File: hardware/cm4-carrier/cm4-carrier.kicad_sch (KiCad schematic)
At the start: 0 parts

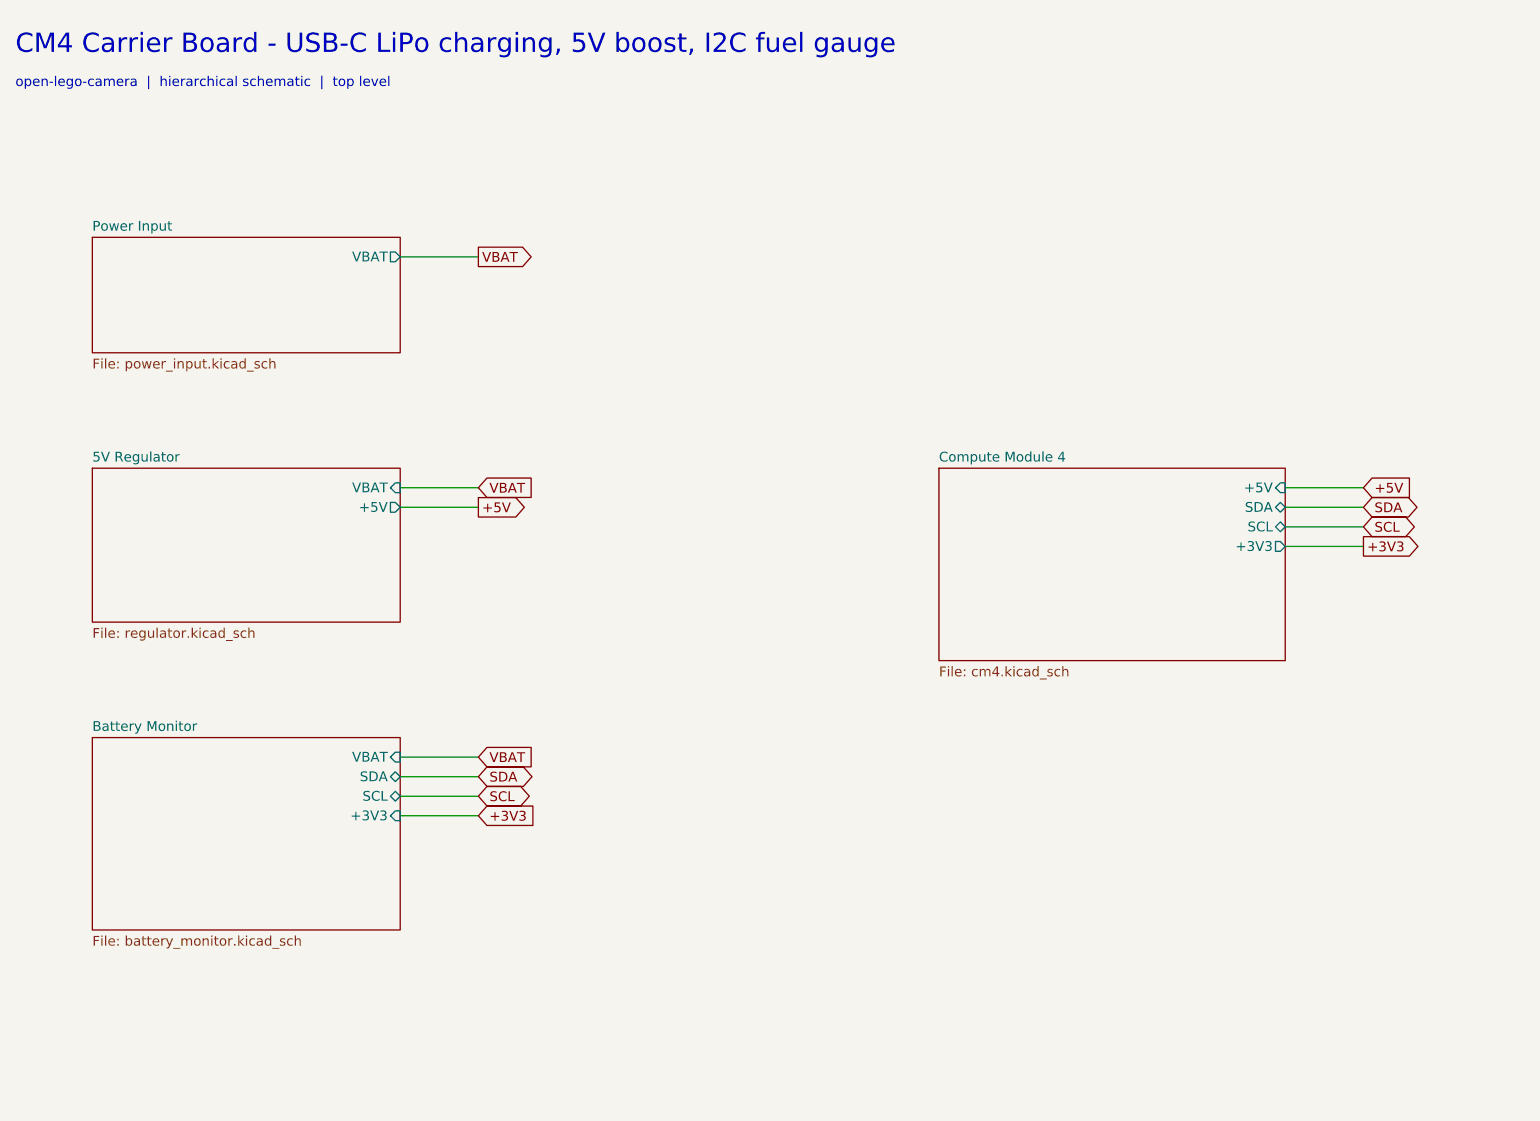
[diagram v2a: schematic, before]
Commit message: Add Dynamic Power Path Management and battery protection
Rework the power architecture to add DPPM and dedicated cell protection.

Power path (DPPM): replace the MCP73831 with a TI BQ24075 USB-friendly
charger whose OUT pin is a separate system rail (SYS). The load now runs
directly from USB when present (system works with a dead/absent battery and
the cell is not needlessly cycled) and falls back to the battery when USB is
removed, while the cell charges from the remaining input budget. Adds ISET,
ILIM and TMR programming resistors, EN1/EN2/CE/SYSOFF strapping, a 10k NTC
on TS for battery-temperature protection, and CHG/PGOOD status LEDs. The
5 V boost regulator now draws from SYS instead of VBAT.

Battery protection: new battery_protection.kicad_sch sub-sheet with an
AP9101CK6 1-cell protection controller (DW01A-class) driving an FS8205A dual
N-MOSFET in the cell's negative line — over-charge, over-discharge,
over-current and short-circuit cutoff. The raw JST cell connector moves here;
its protected terminals feed VBAT/GND to the rest of the board.

Pinouts for BQ24075 and AP9101CK6 were taken from KiCad's Battery_Management
library. Root sheet gains the Battery Protection box and the SYS net; all
hierarchical labels match their sheet pins and reference designators are
globally unique. README/BOM updated. No format change (KiCad 10, 20260306).

Co-Authored-By: Claude Opus 4.8 <noreply@anthropic.com>
Claude-Session: https://claude.ai/code/session_015B7X7FE461jFSRaiTFdnFt
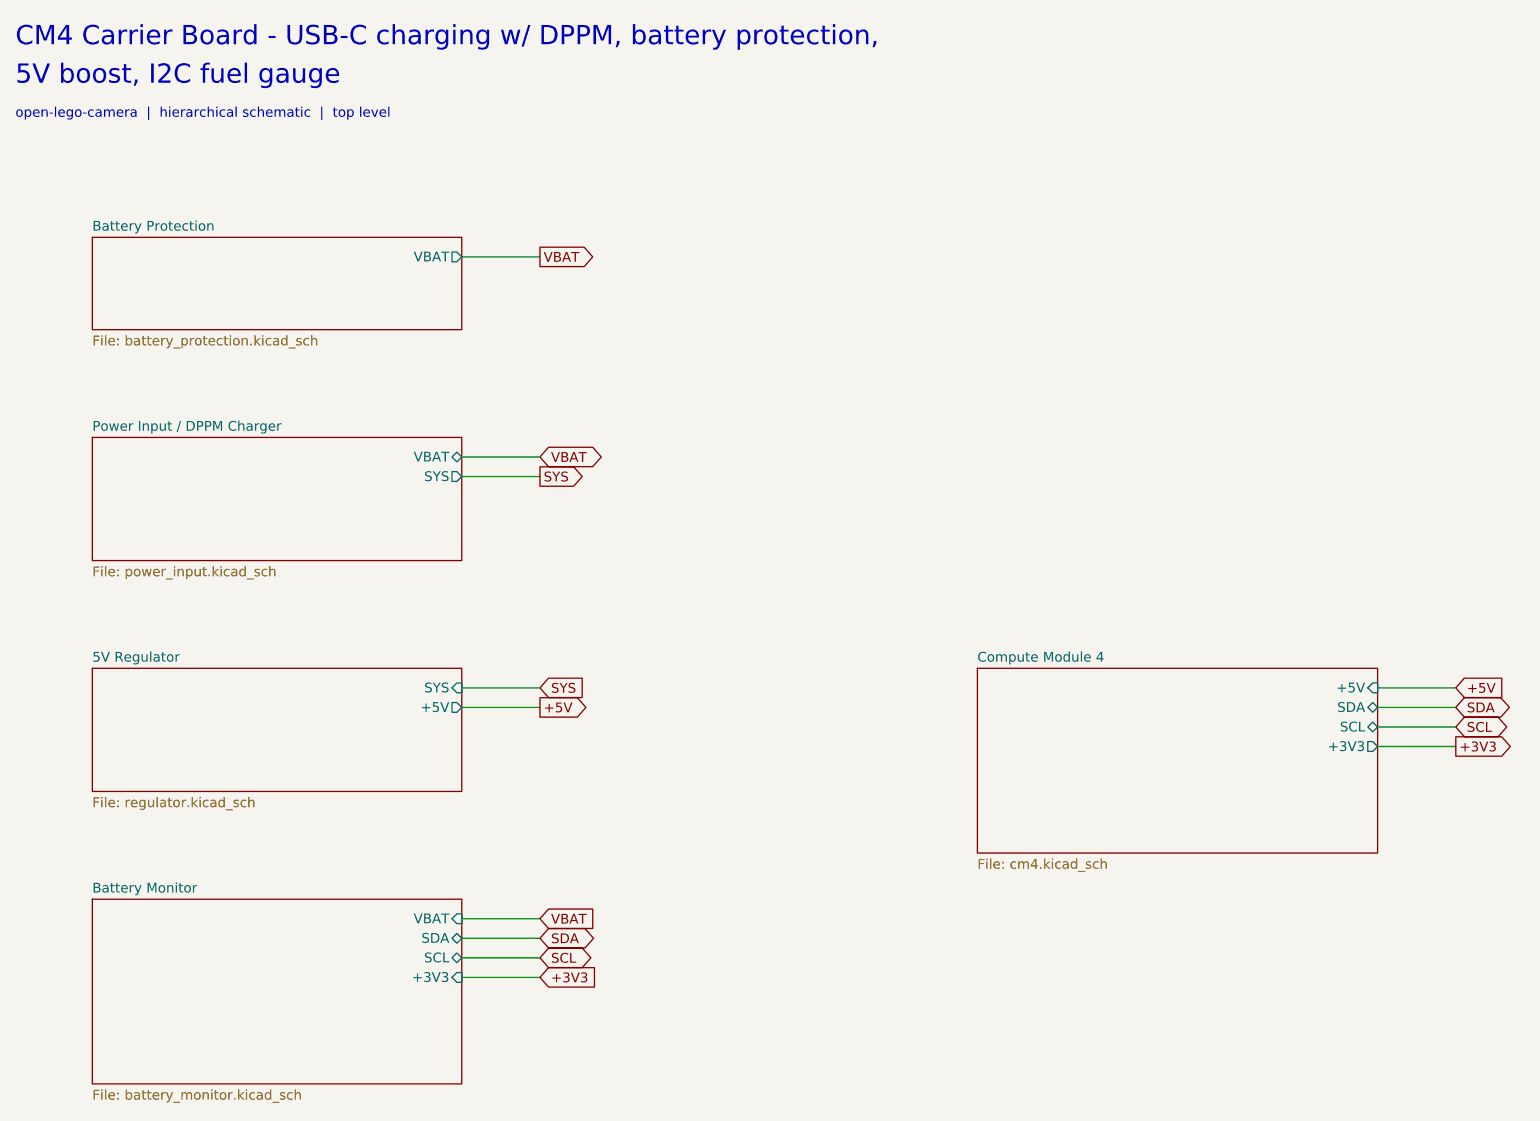
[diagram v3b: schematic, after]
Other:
- removed sheet Power Input
- added sheet Battery Protection (battery_protection.kicad_sch)
- added sheet Power Input / DPPM Charger (power_input.kicad_sch)
- sheet 5V Regulator ports: added SYS; removed VBAT
- note added: "5V boost, I2C fuel gauge"
- note added: "CM4 Carrier Board - USB-C charging w/ DPPM, battery protection,"
- note removed: "CM4 Carrier Board - USB-C LiPo charging, 5V boost, I2C fuel gauge"

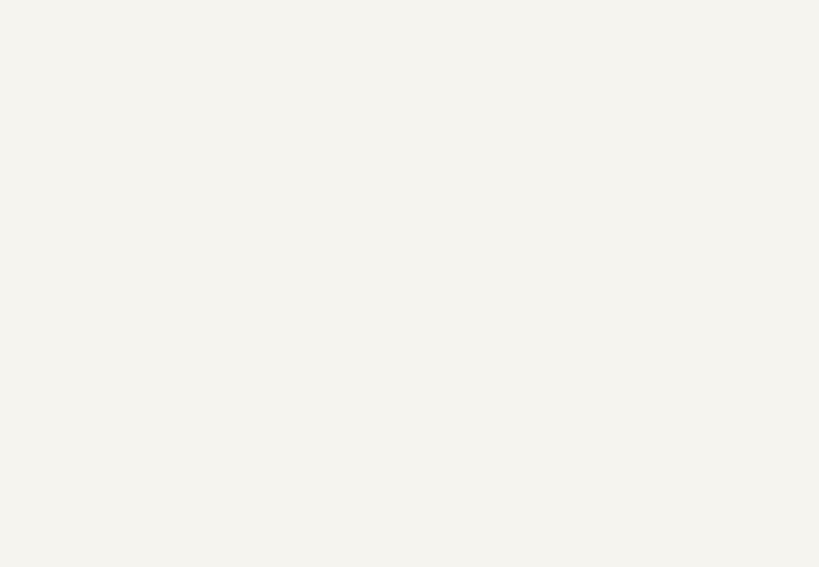
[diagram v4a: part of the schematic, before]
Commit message: Add two CSI-2 cameras with I2C mux and camera 3.3V rail
Add a new cameras.kicad_sch sub-sheet providing two Raspberry Pi CSI-2 camera
interfaces:

- J5 (CSI Camera 0) on the CM4's CAM0 (2-lane) interface; J6 (CSI Camera 1)
  on CAM1 (4-lane, two lanes wired) — standard 15-pin 1.0mm Pi camera FFC
  connectors (Connector_FFC-FPC:JUSHUO_AFA07-S15FCA-00...).
- PCA9544A I2C mux (U5) on the camera control bus I2C0 so the two identical-
  address sensors each sit on their own downstream channel (cam0 = ch0,
  cam1 = ch1, mux at 0x70).
- AP2112K-3.3 LDO (U7) generating a dedicated camera 3.3V rail from +5V, so
  two cameras don't overload the CM4's limited CM4_3.3V_Out. Adds per-channel
  and upstream I2C pull-ups and decoupling (R15-R20, C13-C15).

The CM4 sheet now exports the CAM0/CAM1 MIPI lanes (from J4), I2C0
(I2C_SCL0/SDA0) and four spare GPIOs (GPIO4-7, for the camera IO0/IO1
LED/enable lines) as global nets; the cameras sheet consumes them. Camera
FFC pinout and PCA9544A/DF40/FFC footprints were taken from KiCad's
libraries and the standard 15-pin CSI pinout.

Root gains a (pinless) Cameras sheet box. README/BOM updated. No
schematic-format change (KiCad 10, 20260306).

Co-Authored-By: Claude Opus 4.8 <noreply@anthropic.com>
Claude-Session: https://claude.ai/code/session_015B7X7FE461jFSRaiTFdnFt
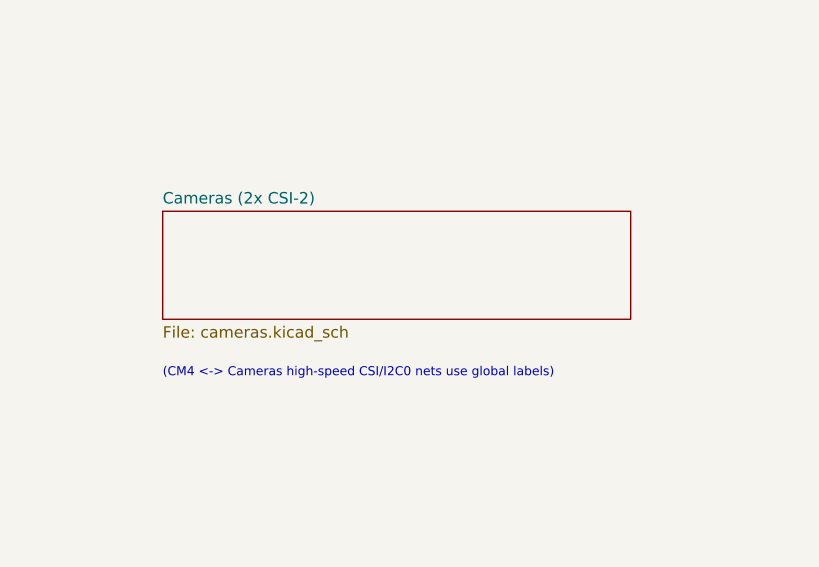
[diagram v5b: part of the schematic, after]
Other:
- added sheet Cameras (2x CSI-2) (cameras.kicad_sch)
- note added: "(CM4 <-> Cameras high-speed CSI/I2C0 nets use global labels)"
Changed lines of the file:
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@@
 		(instances
 			(project "cm4-carrier"
-				(path "/38639fc7-8081-4077-bac3-dd3ee57cf696"
+				(path "/5261f1c5-8601-4e00-981c-a52873d90ff9"
 					(page "6"))))
 	)
@@
 		(instances
 			(project "cm4-carrier"
-				(path "/38639fc7-8081-4077-bac3-dd3ee57cf696"
+				(path "/5261f1c5-8601-4e00-981c-a52873d90ff9"
 					(page "2"))))
 	)
@@
 		(instances
 			(project "cm4-carrier"
-				(path "/38639fc7-8081-4077-bac3-dd3ee57cf696"
+				(path "/5261f1c5-8601-4e00-981c-a52873d90ff9"
 					(page "3"))))
 	)
@@
 		(instances
 			(project "cm4-carrier"
-				(path "/38639fc7-8081-4077-bac3-dd3ee57cf696"
+				(path "/5261f1c5-8601-4e00-981c-a52873d90ff9"
 					(page "4"))))
 	)
@@
 		(instances
 			(project "cm4-carrier"
-				(path "/38639fc7-8081-4077-bac3-dd3ee57cf696"
+				(path "/5261f1c5-8601-4e00-981c-a52873d90ff9"
 					(page "5"))))
 	)
+	(sheet (at 155.00 40.00) (size 52.00 12.00)
+		(exclude_from_sim no) (in_bom yes) (on_board yes) (dnp no)
+		(fields_autoplaced yes)
+		(stroke (width 0.1524) (type solid))
+		(fill (color 0 0 0 0.0000))
+		(property "Sheetname" "Cameras (2x CSI-2)" (at 155.00 39.29 0)
+			(effects (font (size 1.27 1.27)) (justify left bottom)))
+		(property "Sheetfile" "cameras.kicad_sch" (at 155.00 52.71 0)
+			(effects (font (size 1.27 1.27)) (justify left top)))
+		(instances
+			(project "cm4-carrier"
+				(path "/5261f1c5-8601-4e00-981c-a52873d90ff9"
+					(page "7"))))
+	)
+	(text "(CM4 <-> Cameras high-speed CSI/I2C0 nets use global labels)" (at 155.00 58.00 0)
+		(effects (font (size 1.0 1.0)) (justify left))
+)
 	(wire (pts (xy 88.00 42.54) (xy 98.16 42.54))
 		(stroke (width 0) (type default))

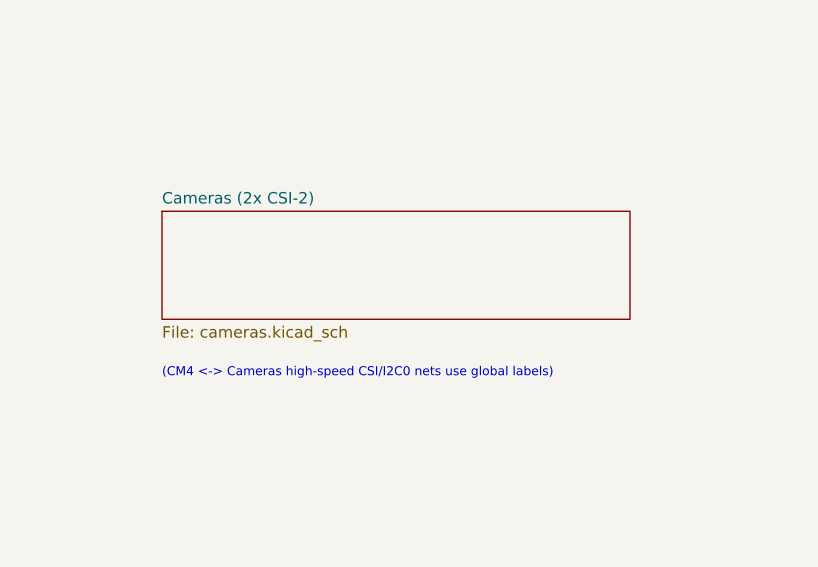
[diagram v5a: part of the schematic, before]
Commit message: Add a DSI display on the CM4's DSI0 interface
Add a Raspberry Pi DSI display connector (J7) to the peripherals sheet
(now "Cameras & Display"):

- J7 is a standard 15-pin 1.0mm RPi FFC driven by the CM4's DSI0 (2-lane)
  interface; the six DSI0 differential lanes are exported from the CM4 sheet
  (J4) as global nets alongside the camera lanes.
- The display's touch/controller I2C shares I2C0 on PCA9544A mux channel 2
  (SD2/SC2, previously unused), with its own pull-ups (R21/R22).
- IO0/IO1 (reset / backlight-enable) route to CM4 GPIO8/GPIO9; 3.3V logic
  comes from the existing camera LDO rail. The 5V panel/backlight power is
  supplied separately, as on the standard RPi 7-inch panel.

The mux is now 3 of 4 channels used (cam0/cam1/display). Root box renamed to
"Cameras & Display". README/BOM updated. No format change (KiCad 10, 20260306).

Co-Authored-By: Claude Opus 4.8 <noreply@anthropic.com>
Claude-Session: https://claude.ai/code/session_015B7X7FE461jFSRaiTFdnFt
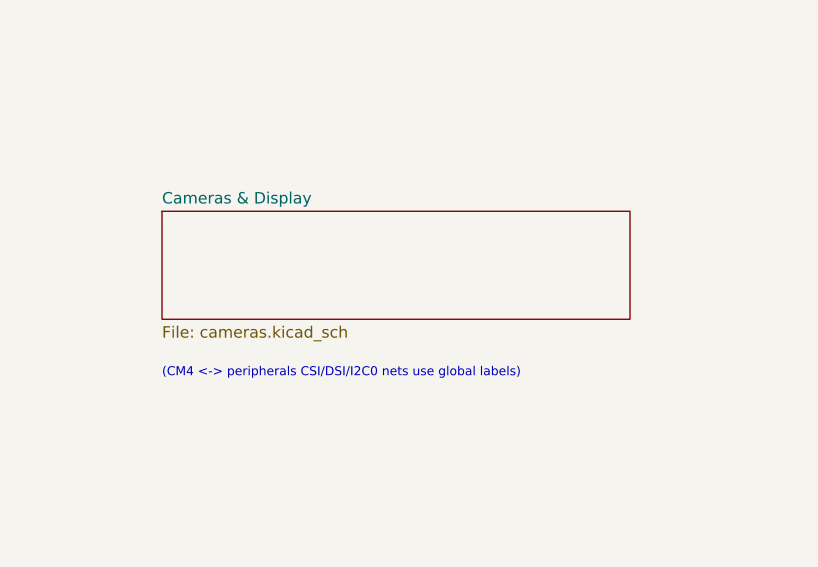
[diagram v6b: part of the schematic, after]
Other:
- removed sheet Cameras (2x CSI-2)
- added sheet Cameras & Display (cameras.kicad_sch)
- note added: "(CM4 <-> peripherals CSI/DSI/I2C0 nets use global labels)"
- note removed: "(CM4 <-> Cameras high-speed CSI/I2C0 nets use global labels)"
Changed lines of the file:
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@@
 		(instances
 			(project "cm4-carrier"
-				(path "/5261f1c5-8601-4e00-981c-a52873d90ff9"
+				(path "/68164e39-daeb-4d86-8c19-ac7cd09b1aca"
 					(page "6"))))
 	)
@@
 		(instances
 			(project "cm4-carrier"
-				(path "/5261f1c5-8601-4e00-981c-a52873d90ff9"
+				(path "/68164e39-daeb-4d86-8c19-ac7cd09b1aca"
 					(page "2"))))
 	)
@@
 		(instances
 			(project "cm4-carrier"
-				(path "/5261f1c5-8601-4e00-981c-a52873d90ff9"
+				(path "/68164e39-daeb-4d86-8c19-ac7cd09b1aca"
 					(page "3"))))
 	)
@@
 		(instances
 			(project "cm4-carrier"
-				(path "/5261f1c5-8601-4e00-981c-a52873d90ff9"
+				(path "/68164e39-daeb-4d86-8c19-ac7cd09b1aca"
 					(page "4"))))
 	)
@@
 		(instances
 			(project "cm4-carrier"
-				(path "/5261f1c5-8601-4e00-981c-a52873d90ff9"
+				(path "/68164e39-daeb-4d86-8c19-ac7cd09b1aca"
 					(page "5"))))
 	)
@@
 		(stroke (width 0.1524) (type solid))
 		(fill (color 0 0 0 0.0000))
-		(property "Sheetname" "Cameras (2x CSI-2)" (at 155.00 39.29 0)
+		(property "Sheetname" "Cameras & Display" (at 155.00 39.29 0)
 			(effects (font (size 1.27 1.27)) (justify left bottom)))
 		(property "Sheetfile" "cameras.kicad_sch" (at 155.00 52.71 0)
@@
 		(instances
 			(project "cm4-carrier"
-				(path "/5261f1c5-8601-4e00-981c-a52873d90ff9"
+				(path "/68164e39-daeb-4d86-8c19-ac7cd09b1aca"
 					(page "7"))))
 	)
-	(text "(CM4 <-> Cameras high-speed CSI/I2C0 nets use global labels)" (at 155.00 58.00 0)
+	(text "(CM4 <-> peripherals CSI/DSI/I2C0 nets use global labels)" (at 155.00 58.00 0)
 		(effects (font (size 1.0 1.0)) (justify left))
 )
